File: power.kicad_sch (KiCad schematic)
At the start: 13 parts, among them J3 USB_C_Receptacle_USB2.0, U10 LTC4054ES5-4.2, U7 MC78M05_TO252, U8 XC6206PxxxMR, U9 SRV05-4

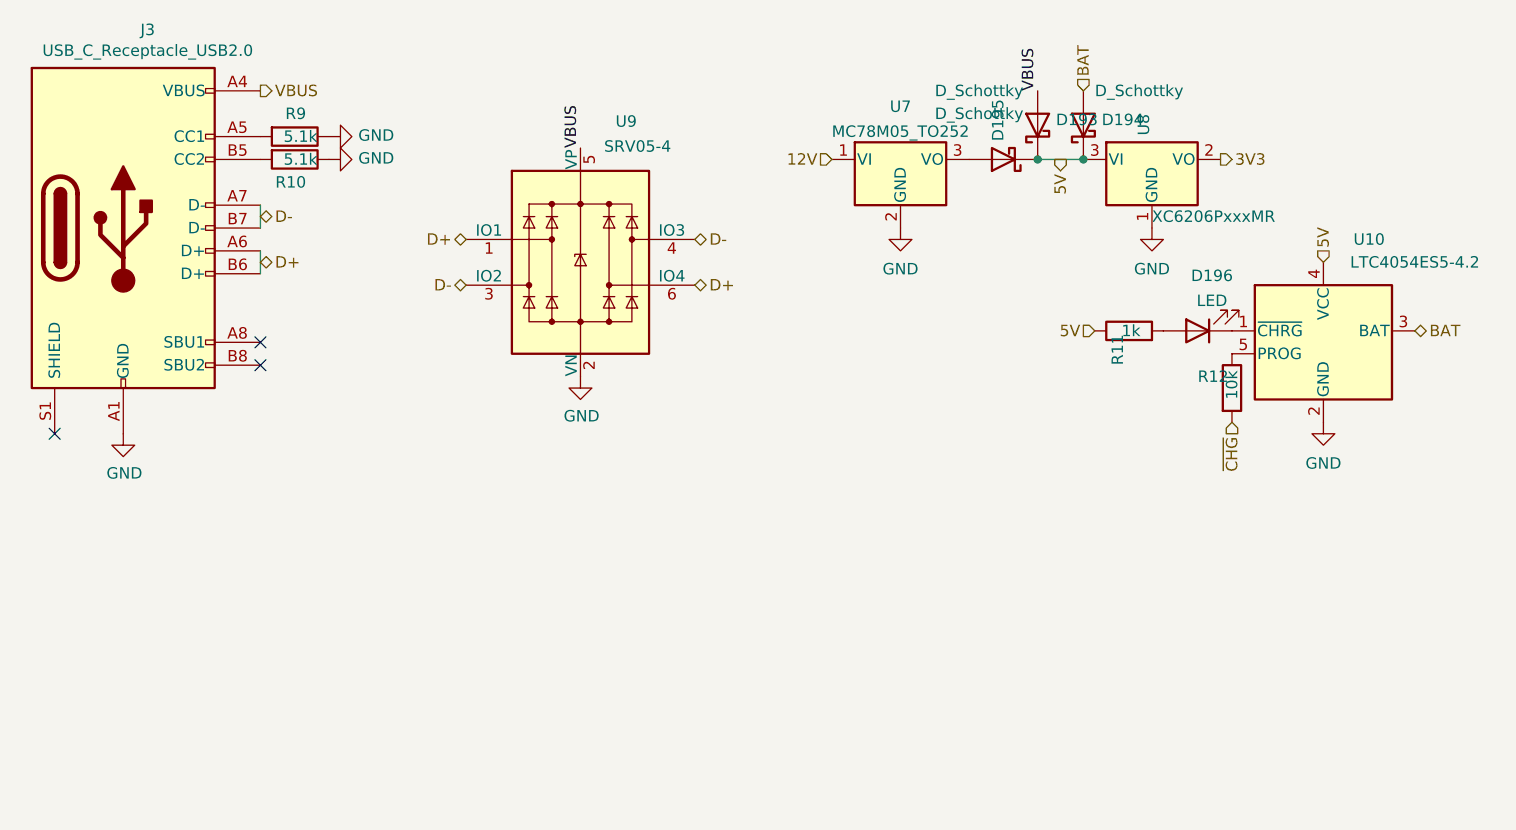
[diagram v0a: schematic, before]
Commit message: routed matrix + PWM driver
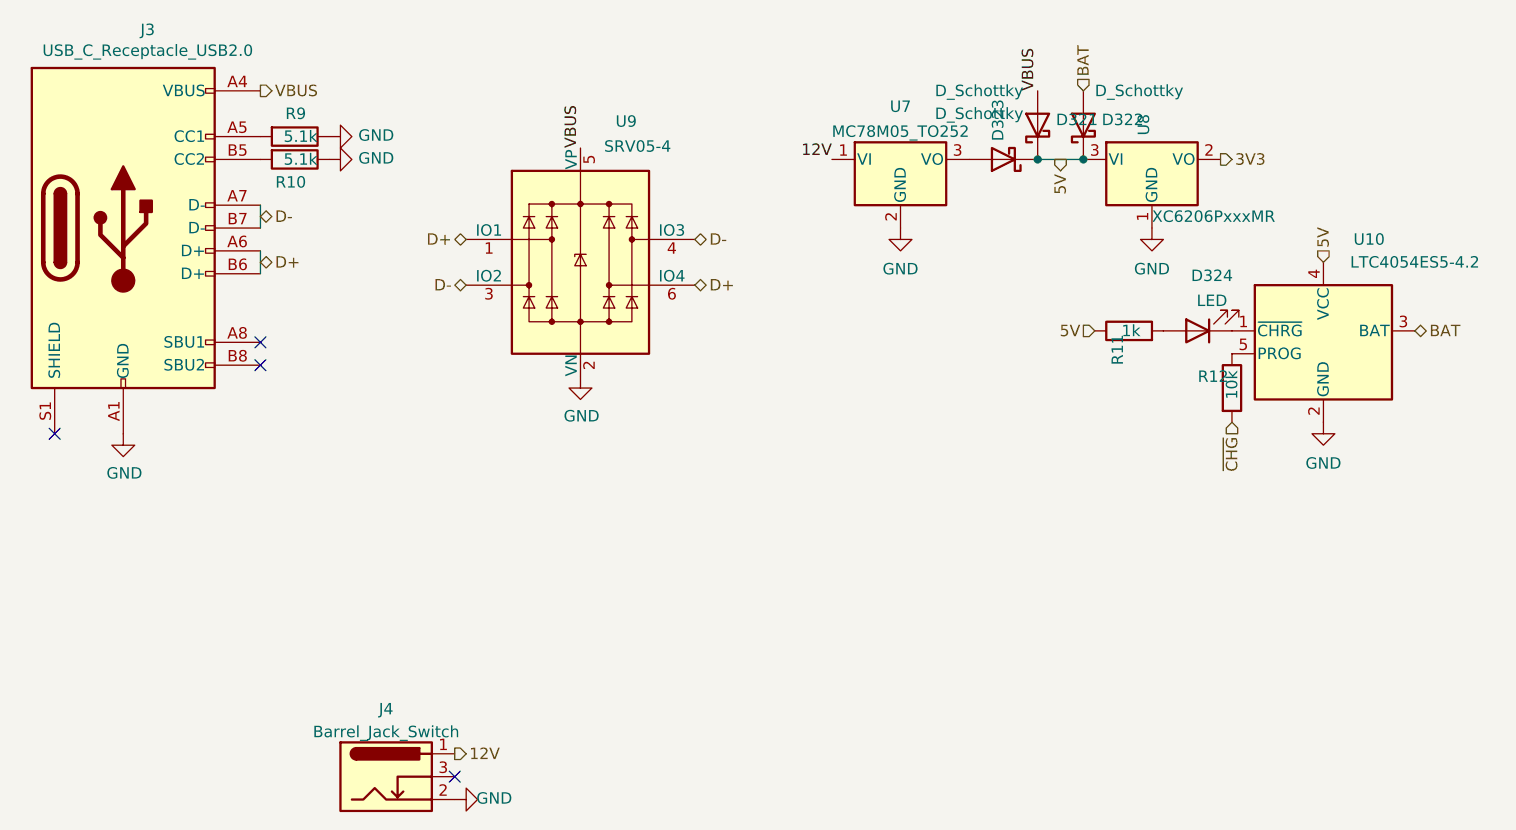
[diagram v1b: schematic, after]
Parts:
- added J4: Barrel_Jack_Switch, Connector_BarrelJack:BarrelJack_CUI_PJ-102AH_Horizontal, symbol Connector:Barrel_Jack_Switch
- renumbered D193 to D321, D194 to D322, D195 to D323, D196 to D324
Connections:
- net 12V: now also J4.1
- net GND: now also J4.2
- no-connect marks 3 -> 4
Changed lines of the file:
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@@
   )
   (no_connect (at 27.94 63.5))
+  (no_connect (at 72.39 101.6))
   (no_connect (at 50.8 55.88))
   (no_connect (at 50.8 53.34))
@@
     (stroke (width 0) (type solid) (color 0 0 0 0))
   )
+  (label "12V" (at 114.3 33.02 180)
+    (effects (font (size 1.27 1.27)) (justify right bottom))
+  )
   (label "VBUS" (at 86.36 31.75 90)
     (effects (font (size 1.27 1.27)) (justify left bottom))
@@
     (effects (font (size 1.27 1.27)) (justify left bottom))
   )
-  (hierarchical_label "12V" (shape input) (at 114.3 33.02 180)
-    (effects (font (size 1.27 1.27)) (justify right))
-  )
   (hierarchical_label "3V3" (shape output) (at 157.48 33.02 0)
     (effects (font (size 1.27 1.27)) (justify left))
@@
   (hierarchical_label "D-" (shape bidirectional) (at 73.66 46.99 180)
     (effects (font (size 1.27 1.27)) (justify right))
+  )
+  (hierarchical_label "12V" (shape output) (at 72.39 99.06 0)
+    (effects (font (size 1.27 1.27)) (justify left))
   )
   (hierarchical_label "D-" (shape bidirectional) (at 99.06 41.91 0)
@@
   (symbol (lib_id "power:GND") (at 58.42 33.02 90) (unit 1)
     (in_bom yes) (on_board yes)
-    (property "Reference" "#PWR0128" (id 0) (at 64.77 33.02 0)
+    (property "Reference" "#PWR030" (id 0) (at 64.77 33.02 0)
       (effects (font (size 1.27 1.27)) hide)
     )
@@
   (symbol (lib_id "Device:D_Schottky") (at 133.35 33.02 180) (unit 1)
     (in_bom yes) (on_board yes)
-    (property "Reference" "D195" (id 0) (at 132.759 30.988 90)
+    (property "Reference" "D323" (id 0) (at 132.759 30.988 90)
       (effects (font (size 1.27 1.27)) (justify right))
     )
@@
   (symbol (lib_id "power:GND") (at 149.86 40.64 0) (unit 1)
     (in_bom yes) (on_board yes) (fields_autoplaced)
-    (property "Reference" "#PWR0125" (id 0) (at 149.86 46.99 0)
+    (property "Reference" "#PWR032" (id 0) (at 149.86 46.99 0)
       (effects (font (size 1.27 1.27)) hide)
     )
@@
   (symbol (lib_id "Device:D_Schottky") (at 142.24 29.21 90) (unit 1)
     (in_bom yes) (on_board yes)
-    (property "Reference" "D194" (id 0) (at 144.272 28.619 90)
+    (property "Reference" "D322" (id 0) (at 144.272 28.619 90)
       (effects (font (size 1.27 1.27)) (justify right))
     )
@@
   (symbol (lib_id "power:GND") (at 168.91 62.23 0) (unit 1)
     (in_bom yes) (on_board yes) (fields_autoplaced)
-    (property "Reference" "#PWR0124" (id 0) (at 168.91 68.58 0)
+    (property "Reference" "#PWR034" (id 0) (at 168.91 68.58 0)
       (effects (font (size 1.27 1.27)) hide)
     )
@@
   (symbol (lib_id "power:GND") (at 58.42 30.48 90) (unit 1)
     (in_bom yes) (on_board yes)
-    (property "Reference" "#PWR0129" (id 0) (at 64.77 30.48 0)
+    (property "Reference" "#PWR029" (id 0) (at 64.77 30.48 0)
       (effects (font (size 1.27 1.27)) hide)
     )
@@
   (symbol (lib_id "power:GND") (at 35.56 63.5 0) (unit 1)
     (in_bom yes) (on_board yes)
-    (property "Reference" "#PWR0127" (id 0) (at 35.56 69.85 0)
+    (property "Reference" "#PWR035" (id 0) (at 35.56 69.85 0)
       (effects (font (size 1.27 1.27)) hide)
     )
@@
   (symbol (lib_id "power:GND") (at 86.36 57.15 0) (unit 1)
     (in_bom yes) (on_board yes)
-    (property "Reference" "#PWR0130" (id 0) (at 86.36 63.5 0)
+    (property "Reference" "#PWR033" (id 0) (at 86.36 63.5 0)
       (effects (font (size 1.27 1.27)) hide)
     )
@@
     (pin "1")
   )
+  (symbol (lib_id "Connector:Barrel_Jack_Switch") (at 64.77 101.6 0) (unit 1)
+    (in_bom yes) (on_board yes) (fields_autoplaced)
+    (property "Reference" "J4" (id 0) (at 64.77 94.0902 0))
+    (property "Value" "Barrel_Jack_Switch" (id 1) (at 64.77 96.6271 0))
+    (property "Footprint" "Connector_BarrelJack:BarrelJack_CUI_PJ-102AH_Horizontal" (id 2) (at 66.04 102.616 0)
+      (effects (font (size 1.27 1.27)) hide)
+    )
+    (property "Datasheet" "~" (id 3) (at 66.04 102.616 0)
+      (effects (font (size 1.27 1.27)) hide)
+    )
+    (pin "1")
+    (pin "2")
+    (pin "3")
+  )
   (symbol (lib_id "Device:R") (at 54.61 30.48 270) (unit 1)
     (in_bom yes) (on_board yes)
@@
   (symbol (lib_id "Device:D_Schottky") (at 137.16 29.21 90) (unit 1)
     (in_bom yes) (on_board yes)
-    (property "Reference" "D193" (id 0) (at 139.192 28.619 90)
+    (property "Reference" "D321" (id 0) (at 139.192 28.619 90)
       (effects (font (size 1.27 1.27)) (justify right))
     )
@@
     (pin "1")
     (pin "2")
+  )
+  (symbol (lib_id "power:GND") (at 72.39 104.14 90) (unit 1)
+    (in_bom yes) (on_board yes)
+    (property "Reference" "#PWR0107" (id 0) (at 78.74 104.14 0)
+      (effects (font (size 1.27 1.27)) hide)
+    )
+    (property "Value" "GND" (id 1) (at 76.7842 104.013 90))
+    (property "Footprint" "" (id 2) (at 72.39 104.14 0)
+      (effects (font (size 1.27 1.27)) hide)
+    )
+    (property "Datasheet" "" (id 3) (at 72.39 104.14 0)
+      (effects (font (size 1.27 1.27)) hide)
+    )
+    (pin "1")
   )
   (symbol (lib_id "Battery_Management:LTC4054ES5-4.2") (at 168.91 52.07 0) (unit 1)
@@
   (symbol (lib_id "power:GND") (at 121.92 40.64 0) (unit 1)
     (in_bom yes) (on_board yes) (fields_autoplaced)
-    (property "Reference" "#PWR0126" (id 0) (at 121.92 46.99 0)
+    (property "Reference" "#PWR031" (id 0) (at 121.92 46.99 0)
       (effects (font (size 1.27 1.27)) hide)
     )
@@
   (symbol (lib_id "Device:LED") (at 154.94 52.07 180) (unit 1)
     (in_bom yes) (on_board yes) (fields_autoplaced)
-    (property "Reference" "D196" (id 0) (at 156.5275 45.9445 0))
+    (property "Reference" "D324" (id 0) (at 156.5275 45.9445 0))
     (property "Value" "LED" (id 1) (at 156.5275 48.7196 0))
     (property "Footprint" "Diode_SMD:D_0805_2012Metric" (id 2) (at 154.94 52.07 0)

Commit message: routed PMU
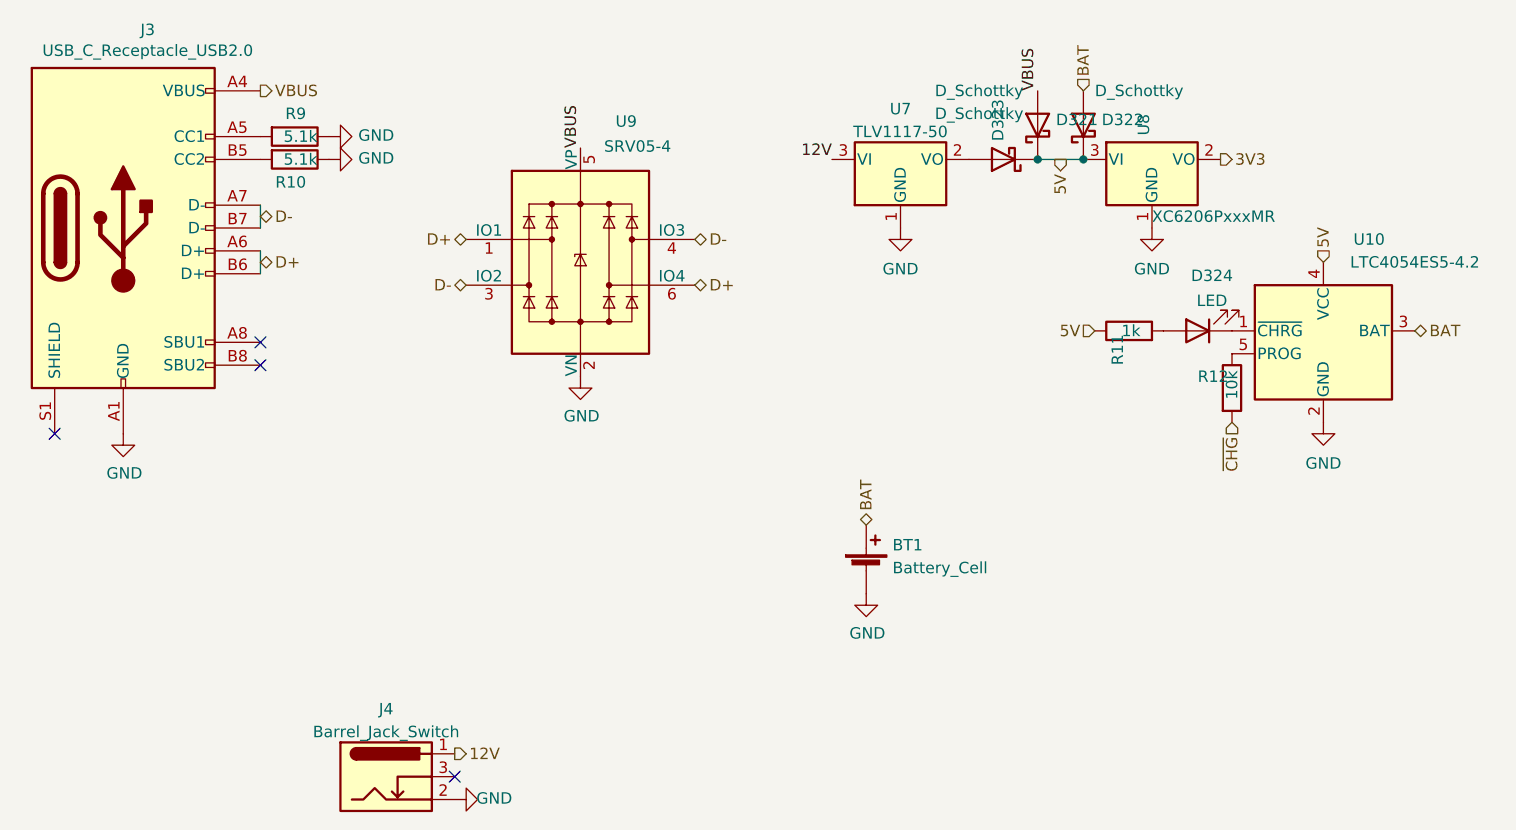
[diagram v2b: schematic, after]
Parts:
- removed U7: MC78M05_TO252, Package_TO_SOT_SMD:TO-252-2, symbol Regulator_Linear:MC78M05_TO252
- added BT1: Battery_Cell, Connector_JST:JST_PH_S2B-PH-SM4-TB_1x02-1MP_P2.00mm_Horizontal, symbol Device:Battery_Cell
- added U7: TLV1117-50, Package_TO_SOT_SMD:SOT-223, symbol Regulator_Linear:TLV1117-50
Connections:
- net 12V: now also U7.3 (VI)
- net BAT: now also BT1.1 (+)
- net GND: now also BT1.2 (-), U7.1 (GND)
- net at D323.2 (A): now also U7.2 (VO)
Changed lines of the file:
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@@
+    (effects (font (size 1.27 1.27)) (justify left))
+  )
+  (hierarchical_label "BAT" (shape bidirectional) (at 118.11 73.66 90)
     (effects (font (size 1.27 1.27)) (justify left))
   )
@@
     (pin "2")
   )
-  (symbol (lib_id "Regulator_Linear:MC78M05_TO252") (at 121.92 33.02 0) (unit 1)
-    (in_bom yes) (on_board yes) (fields_autoplaced)
-    (property "Reference" "U7" (id 0) (at 121.92 27.1485 0))
-    (property "Value" "MC78M05_TO252" (id 1) (at 121.92 29.9236 0))
-    (property "Footprint" "Package_TO_SOT_SMD:TO-252-2" (id 2) (at 121.92 27.305 0)
-      (effects (font (size 1.27 1.27) italic) hide)
-    )
-    (property "Datasheet" "https://www.onsemi.com/pub/Collateral/MC78M00-D.PDF" (id 3) (at 121.92 34.29 0)
-      (effects (font (size 1.27 1.27)) hide)
-    )
-    (pin "1")
-    (pin "2")
-    (pin "3")
-  )
   (symbol (lib_id "power:GND") (at 168.91 62.23 0) (unit 1)
     (in_bom yes) (on_board yes) (fields_autoplaced)
@@
     (pin "1")
   )
+  (symbol (lib_id "power:GND") (at 118.11 81.28 0) (unit 1)
+    (in_bom yes) (on_board yes)
+    (property "Reference" "#PWR0111" (id 0) (at 118.11 87.63 0)
+      (effects (font (size 1.27 1.27)) hide)
+    )
+    (property "Value" "GND" (id 1) (at 118.237 85.6742 0))
+    (property "Footprint" "" (id 2) (at 118.11 81.28 0)
+      (effects (font (size 1.27 1.27)) hide)
+    )
+    (property "Datasheet" "" (id 3) (at 118.11 81.28 0)
+      (effects (font (size 1.27 1.27)) hide)
+    )
+    (pin "1")
+  )
   (symbol (lib_id "power:GND") (at 58.42 30.48 90) (unit 1)
     (in_bom yes) (on_board yes)
@@
     )
     (pin "1")
+  )
+  (symbol (lib_id "Device:Battery_Cell") (at 118.11 78.74 0) (unit 1)
+    (in_bom yes) (on_board yes) (fields_autoplaced)
+    (property "Reference" "BT1" (id 0) (at 121.031 75.8733 0)
+      (effects (font (size 1.27 1.27)) (justify left))
+    )
+    (property "Value" "Battery_Cell" (id 1) (at 121.031 78.4102 0)
+      (effects (font (size 1.27 1.27)) (justify left))
+    )
+    (property "Footprint" "Connector_JST:JST_PH_S2B-PH-SM4-TB_1x02-1MP_P2.00mm_Horizontal" (id 2) (at 118.11 77.216 90)
+      (effects (font (size 1.27 1.27)) hide)
+    )
+    (property "Datasheet" "~" (id 3) (at 118.11 77.216 90)
+      (effects (font (size 1.27 1.27)) hide)
+    )
+    (pin "1")
+    (pin "2")
   )
   (symbol (lib_id "power:GND") (at 35.56 63.5 0) (unit 1)
@@
     (pin "2")
   )
+  (symbol (lib_id "Regulator_Linear:TLV1117-50") (at 121.92 33.02 0) (unit 1)
+    (in_bom yes) (on_board yes) (fields_autoplaced)
+    (property "Reference" "U7" (id 0) (at 121.92 27.4152 0))
+    (property "Value" "TLV1117-50" (id 1) (at 121.92 29.9521 0))
+    (property "Footprint" "Package_TO_SOT_SMD:SOT-223" (id 2) (at 121.92 33.02 0)
+      (effects (font (size 1.27 1.27)) hide)
+    )
+    (property "Datasheet" "http://www.ti.com/lit/ds/symlink/tlv1117.pdf" (id 3) (at 121.92 33.02 0)
+      (effects (font (size 1.27 1.27)) hide)
+    )
+    (pin "1")
+    (pin "2")
+    (pin "3")
+  )
   (symbol (lib_id "Device:D_Schottky") (at 137.16 29.21 90) (unit 1)

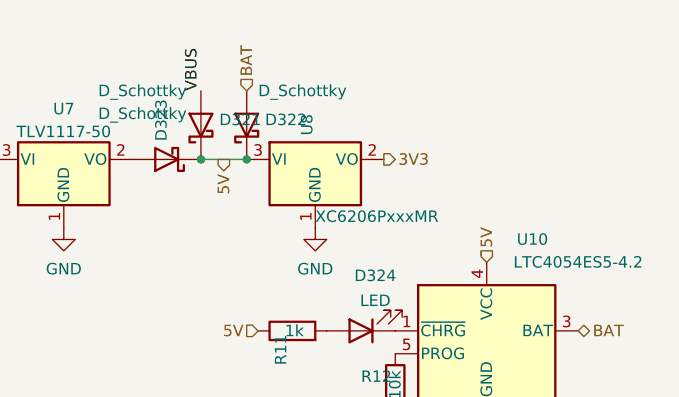
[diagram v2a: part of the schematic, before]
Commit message: routed all LED + PMU
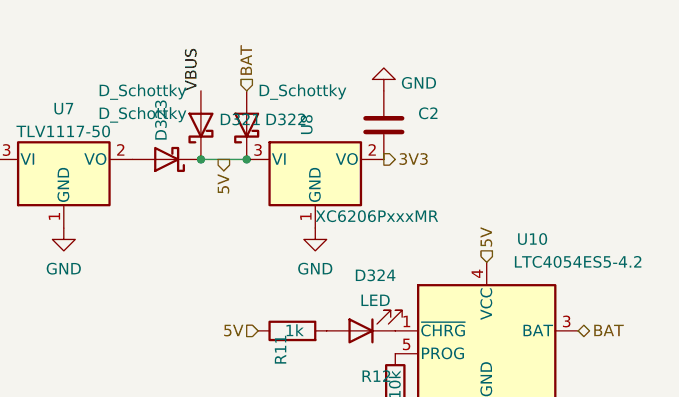
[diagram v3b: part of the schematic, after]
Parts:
- added C2: (no value), Capacitor_SMD:C_0603_1608Metric, symbol Device:C
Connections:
- net 3V3: now also C2.2
- net GND: now also C2.1
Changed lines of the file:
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@@
     (pin "2")
+  )
+  (symbol (lib_id "power:GND") (at 157.48 25.4 180) (unit 1)
+    (in_bom yes) (on_board yes) (fields_autoplaced)
+    (property "Reference" "#PWR036" (id 0) (at 157.48 19.05 0)
+      (effects (font (size 1.27 1.27)) hide)
+    )
+    (property "Value" "GND" (id 1) (at 159.385 24.5638 0)
+      (effects (font (size 1.27 1.27)) (justify right))
+    )
+    (property "Footprint" "" (id 2) (at 157.48 25.4 0)
+      (effects (font (size 1.27 1.27)) hide)
+    )
+    (property "Datasheet" "" (id 3) (at 157.48 25.4 0)
+      (effects (font (size 1.27 1.27)) hide)
+    )
+    (pin "1")
   )
   (symbol (lib_id "power:GND") (at 168.91 62.23 0) (unit 1)
@@
       (effects (font (size 1.27 1.27)) hide)
     )
+    (pin "1")
+    (pin "2")
+  )
+  (symbol (lib_id "Device:C") (at 157.48 29.21 0) (unit 1)
+    (in_bom yes) (on_board yes)
+    (property "Reference" "C2" (id 0) (at 161.29 27.94 0)
+      (effects (font (size 1.27 1.27)) (justify left))
+    )
+    (property "Value" "" (id 1) (at 161.29 30.48 0)
+      (effects (font (size 1.27 1.27)) (justify left))
+    )
+    (property "Footprint" "Capacitor_SMD:C_0603_1608Metric" (id 2) (at 158.4452 33.02 0)
+      (effects (font (size 1.27 1.27)) hide)
+    )
+    (property "Datasheet" "~" (id 3) (at 157.48 29.21 0)
+      (effects (font (size 1.27 1.27)) hide)
+    )

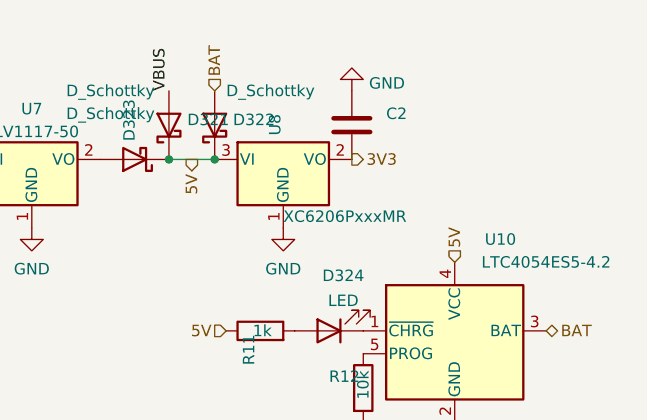
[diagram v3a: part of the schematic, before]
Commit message: rid of LED driver resistors
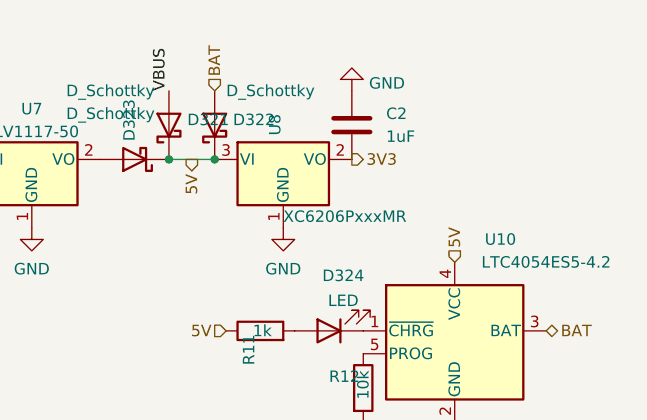
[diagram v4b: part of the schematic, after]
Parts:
- C2: value (none) -> 1uF
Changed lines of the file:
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@@
       (effects (font (size 1.27 1.27)) (justify left))
     )
-    (property "Value" "" (id 1) (at 161.29 30.48 0)
+    (property "Value" "1uF" (id 1) (at 161.29 30.48 0)
       (effects (font (size 1.27 1.27)) (justify left))
     )
